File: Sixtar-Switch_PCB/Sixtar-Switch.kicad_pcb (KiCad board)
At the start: 2 copper layers, 240 x 107 mm, 75 parts, among them J1 USB_C_Receptacle, SW1 KEYSW, SW10 KEYSW, SW11 KEYSW, SW12 KEYSW, SW13 KEYSW, SW14 KEYSW, SW15 KEYSW, SW16 KEYSW, SW17 KEYSW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

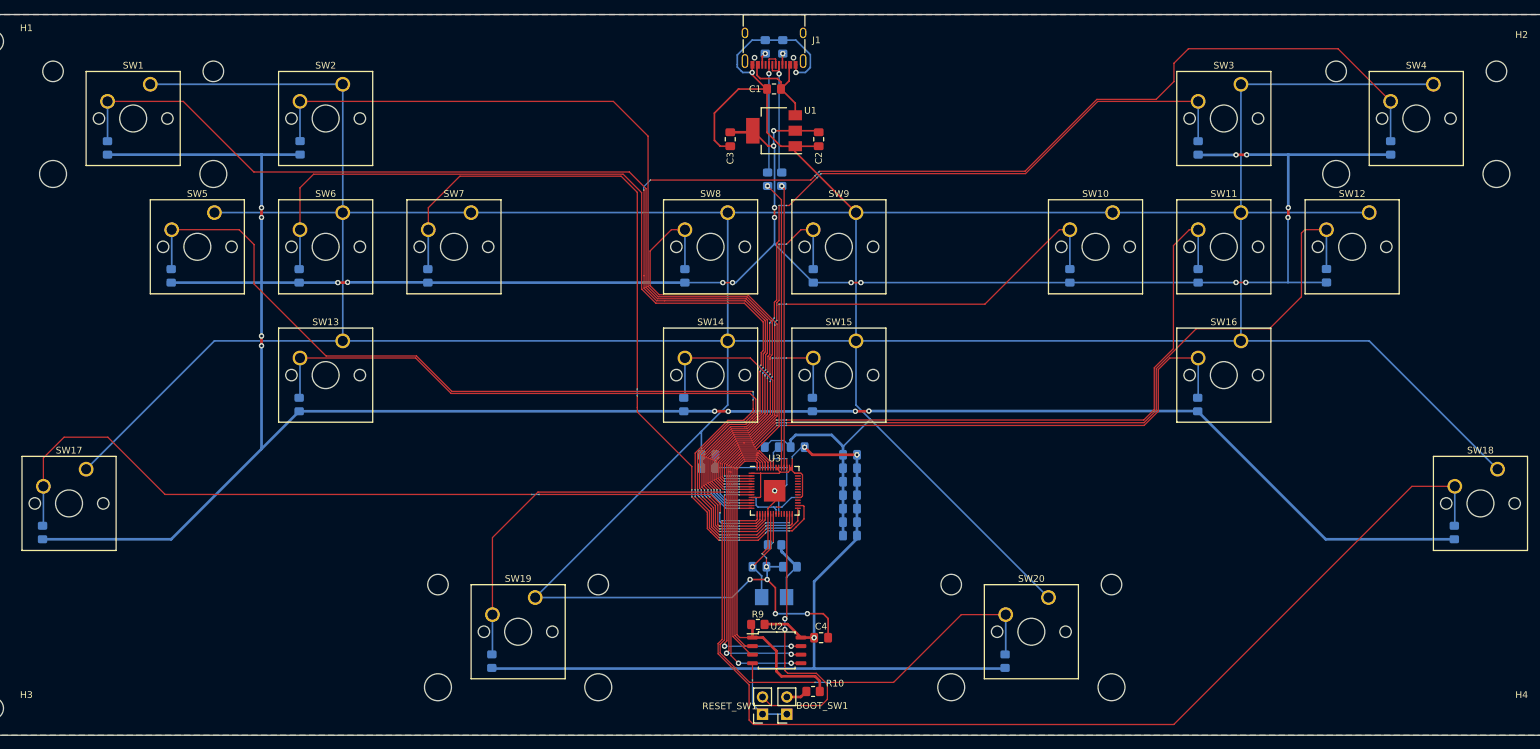
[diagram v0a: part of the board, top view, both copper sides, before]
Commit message: PCB via hole 잘못되서 처음부터 다시 라인 작업해야함
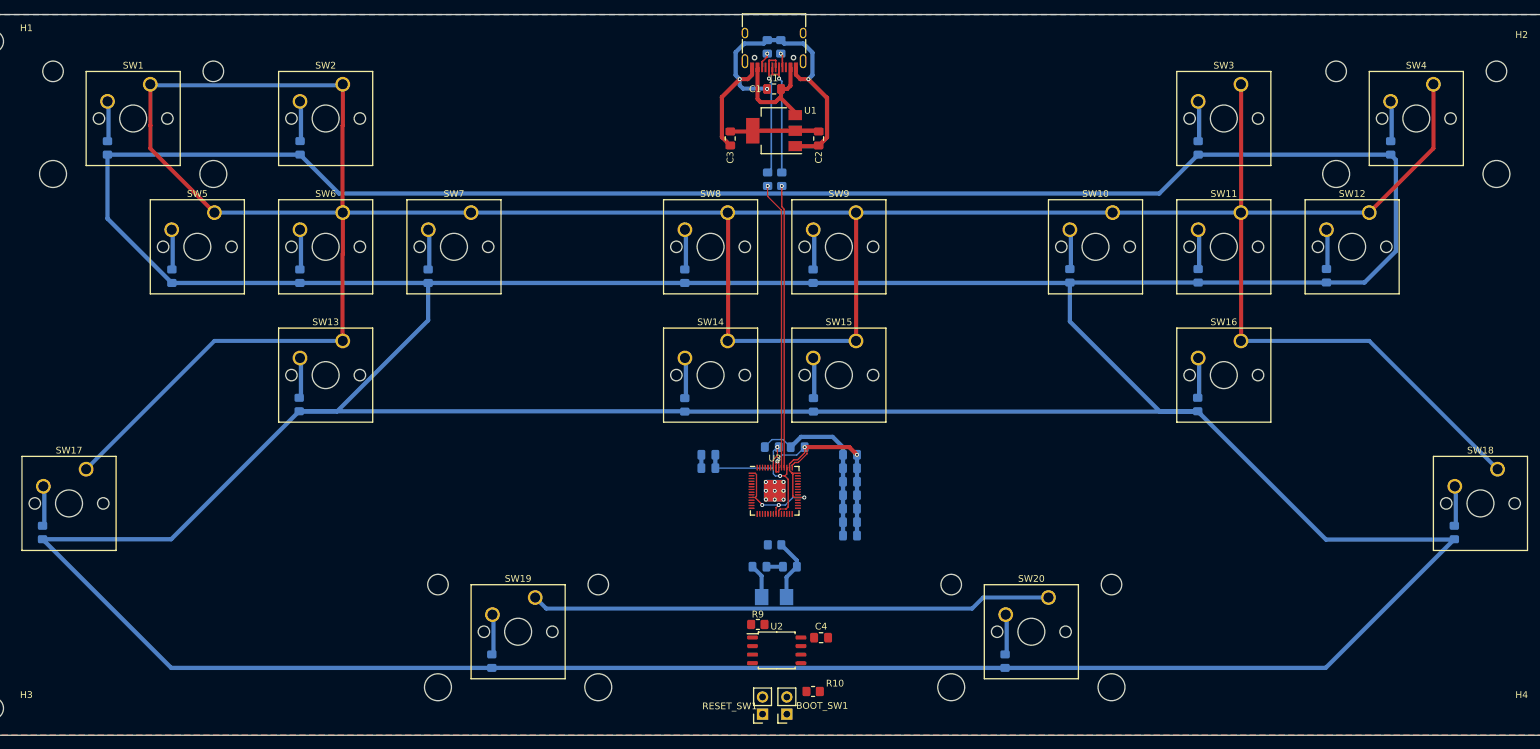
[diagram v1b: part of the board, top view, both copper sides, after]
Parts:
- J1: footprint Connector_USB:USB_C_Receptacle_XKB_U262-16XN-4BVC11 -> Connector_USB:USB_C_Receptacle_HRO_TYPE-C-31-M-12
- moved R2 0.30 mm to (139.0, 22.8)
- moved R3 0.30 mm to (137.0, 22.8)
- moved R15 0.16 mm to (124.8, 76.0)
- moved R16 0.16 mm to (143.8, 76.0)
- moved R26 0.11 mm to (48.6, 56.9)
- moved R24 0.11 mm to (67.6, 56.9)
- moved C2 0.11 mm to (144.6, 36.4)
- moved C3 0.11 mm to (131.5, 36.4)
- moved R27 0.07 mm to (86.7, 56.9)
- moved R12 0.05 mm to (143.8, 56.9)
- moved R11 0.05 mm to (124.8, 56.9)
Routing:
- net +3.3V: track 712.6 -> 1001.3 mm, vias 33 -> 6
- net BTN_RXAxis: track 210.7 -> 6.03 mm, vias 10 -> 0
- net GND: track 860.2 -> 663.0 mm
- net BTN_LXAxis: track 170.4 -> 6.03 mm, vias 6 -> 0
- net BTN_Home: track 163.4 -> 6.01 mm, vias 2 -> 0
- net DPad_Up: track 149.1 -> 6.04 mm, vias 8 -> 0
- net DPad_Left: track 148.3 -> 6.02 mm, vias 8 -> 0
- net BTN_LS: track 140.1 -> 6.02 mm, vias 4 -> 0
- net BTN_RS: track 130.4 -> 6.03 mm, vias 10 -> 0
- net BTN_A: track 126.5 -> 5.96 mm, vias 4 -> 0
- net BTN_Capture: track 125.8 -> 6.03 mm, vias 4 -> 0
- net DPad_Right: track 116.6 -> 6.04 mm, vias 8 -> 0
- net DPad_Down: track 115.6 -> 6.08 mm, vias 6 -> 0
- net BTN_X: track 111.8 -> 5.97 mm, vias 4 -> 0
- net BTN_B: track 93.2 -> 6.06 mm, vias 4 -> 0
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
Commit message: 배선 수정 및 via hole 수정
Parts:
- J1: footprint Connector_USB:USB_C_Receptacle_HRO_TYPE-C-31-M-12 -> Connector_USB:USB_C_Receptacle_GCT_USB4105-xx-A_16P_TopMnt_Horizontal
- moved R10 0.20 mm to (143.6, 118.5)
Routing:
- net BTN_RXAxis: track 6.03 -> 206.8 mm, vias 0 -> 10
- net DPad_Left: track 6.02 -> 177.4 mm, vias 0 -> 8
- net BTN_LXAxis: track 6.03 -> 174.8 mm, vias 0 -> 6
- net BTN_RS: track 6.03 -> 161.2 mm, vias 0 -> 10
- net BTN_Home: track 6.01 -> 160.7 mm, vias 0 -> 6
- net BTN_A: track 5.96 -> 140.7 mm, vias 0 -> 4
- net BTN_LS: track 6.02 -> 138.1 mm, vias 0 -> 2
- net DPad_Up: track 6.04 -> 134.5 mm, vias 0 -> 2
- net DPad_Right: track 6.04 -> 132.8 mm, vias 0 -> 8
- net BTN_Capture: track 6.03 -> 131.4 mm, vias 0 -> 4
- net GND: track 663.0 -> 787.3 mm, vias 12 -> 36
- net BTN_X: track 5.97 -> 108.9 mm, vias 0 -> 4
- net DPad_Down: track 6.08 -> 101.2 mm, vias 0 -> 2
- net +3.3V: track 1001.3 -> 1091.9 mm, vias 6 -> 9
- net BTN_B: track 6.06 -> 92.7 mm, vias 0 -> 4
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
